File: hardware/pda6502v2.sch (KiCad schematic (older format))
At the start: 0 parts

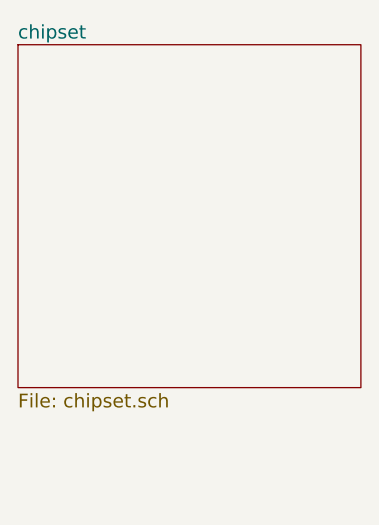
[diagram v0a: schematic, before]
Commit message: hardware: chipset hierarchical pins
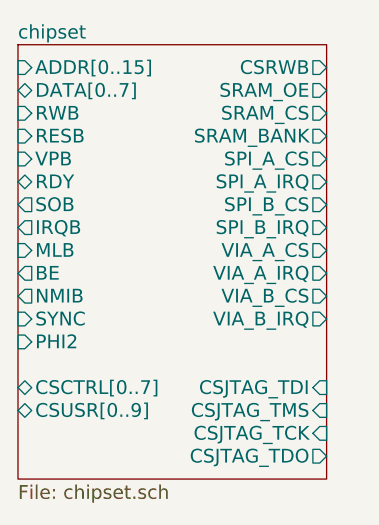
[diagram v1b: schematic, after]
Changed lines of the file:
@@
 $EndDescr
 $Sheet
-S 3400 2200 1500 1500
+S 3400 2200 1350 1900
 U 58EB910B
 F0 "chipset" 60
 F1 "chipset.sch" 60
+F2 "ADDR[0..15]" I L 3400 2300 60
+F3 "CSCTRL[0..7]" B L 3400 3700 60
+F4 "CSUSR[0..9]" B L 3400 3800 60
+F5 "RESB" I L 3400 2600 60
+F6 "VPB" I L 3400 2700 60
+F7 "RDY" B L 3400 2800 60
+F8 "SOB" O L 3400 2900 60
+F9 "IRQB" O L 3400 3000 60
+F10 "MLB" I L 3400 3100 60
+F11 "BE" O L 3400 3200 60
+F12 "NMIB" O L 3400 3300 60
+F13 "SYNC" I L 3400 3400 60
+F14 "RWB" I L 3400 2500 60
+F15 "PHI2" I L 3400 3500 60
+F16 "CSRWB" O R 4750 2300 60
+F17 "SRAM_OE" O R 4750 2400 60
+F18 "SRAM_CS" O R 4750 2500 60
+F19 "SRAM_BANK" O R 4750 2600 60
+F20 "SPI_A_CS" O R 4750 2700 60
+F21 "SPI_A_IRQ" O R 4750 2800 60
+F22 "SPI_B_CS" O R 4750 2900 60
+F23 "SPI_B_IRQ" O R 4750 3000 60
+F24 "VIA_A_CS" O R 4750 3100 60
+F25 "VIA_A_IRQ" O R 4750 3200 60
+F26 "VIA_B_CS" O R 4750 3300 60
+F27 "VIA_B_IRQ" O R 4750 3400 60
+F28 "CSJTAG_TDI" I R 4750 3700 60
+F29 "CSJTAG_TMS" I R 4750 3800 60
+F30 "CSJTAG_TCK" I R 4750 3900 60
+F31 "CSJTAG_TDO" O R 4750 4000 60
+F32 "DATA[0..7]" B L 3400 2400 60
 $EndSheet
 $EndSCHEMATC

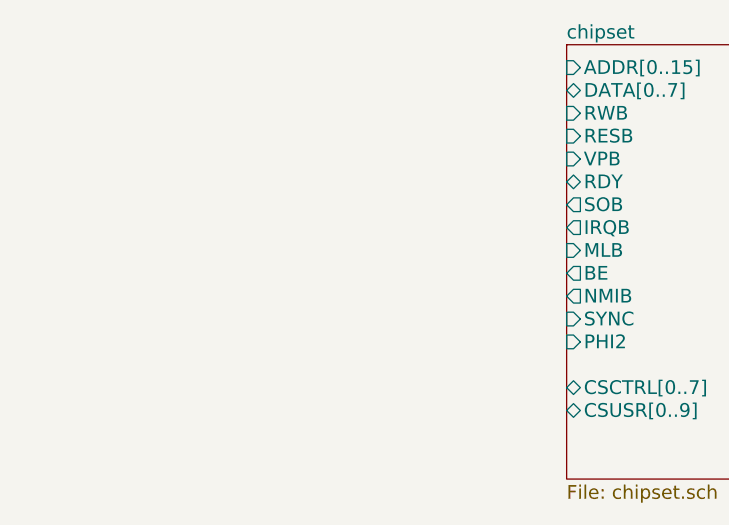
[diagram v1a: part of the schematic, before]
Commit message: hardware: CPU sub-schematic.
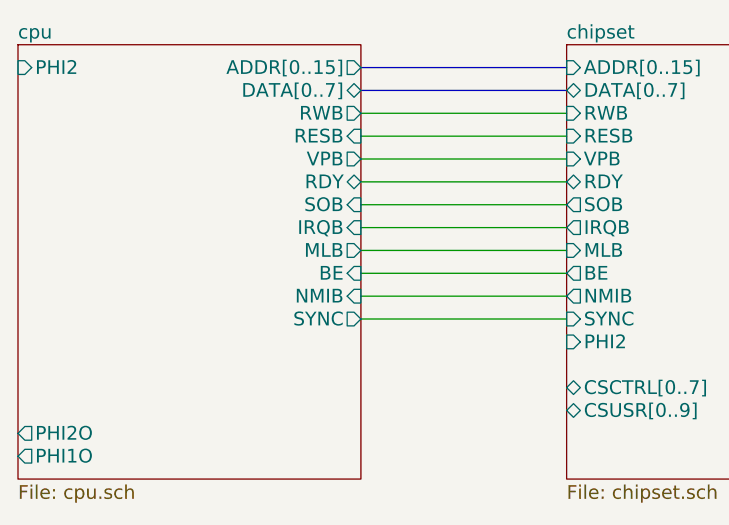
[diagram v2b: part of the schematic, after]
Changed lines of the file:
@@
 $Descr A4 11693 8268
 encoding utf-8
-Sheet 1 2
+Sheet 1 3
 Title ""
 Date ""
@@
 F32 "DATA[0..7]" B L 3400 2400 60
 $EndSheet
+$Sheet
+S 1000 2200 1500 1900
+U 58ED7217
+F0 "cpu" 60
+F1 "cpu.sch" 60
+F2 "ADDR[0..15]" O R 2500 2300 60
+F3 "DATA[0..7]" B R 2500 2400 60
+F4 "VPB" O R 2500 2700 60
+F5 "RDY" B R 2500 2800 60
+F6 "PHI1O" O L 1000 4000 60
+F7 "IRQB" I R 2500 3000 60
+F8 "MLB" O R 2500 3100 60
+F9 "NMIB" I R 2500 3300 60
+F10 "SYNC" O R 2500 3400 60
+F11 "RESB" I R 2500 2600 60
+F12 "PHI2O" O L 1000 3900 60
+F13 "SOB" I R 2500 2900 60
+F14 "PHI2" I L 1000 2300 60
+F15 "BE" I R 2500 3200 60
+F16 "RWB" O R 2500 2500 60
+$EndSheet
+Wire Bus Line
+	2500 2300 3400 2300
+Wire Bus Line
+	2500 2400 3400 2400
+Wire Wire Line
+	2500 2500 3400 2500
+Wire Wire Line
+	2500 2600 3400 2600
+Wire Wire Line
+	2500 2700 3400 2700
+Wire Wire Line
+	2500 2800 3400 2800
+Wire Wire Line
+	2500 2900 3400 2900
+Wire Wire Line
+	2500 3000 3400 3000
+Wire Wire Line
+	2500 3100 3400 3100
+Wire Wire Line
+	2500 3200 3400 3200
+Wire Wire Line
+	2500 3300 3400 3300
+Wire Wire Line
+	2500 3400 3400 3400
 $EndSCHEMATC

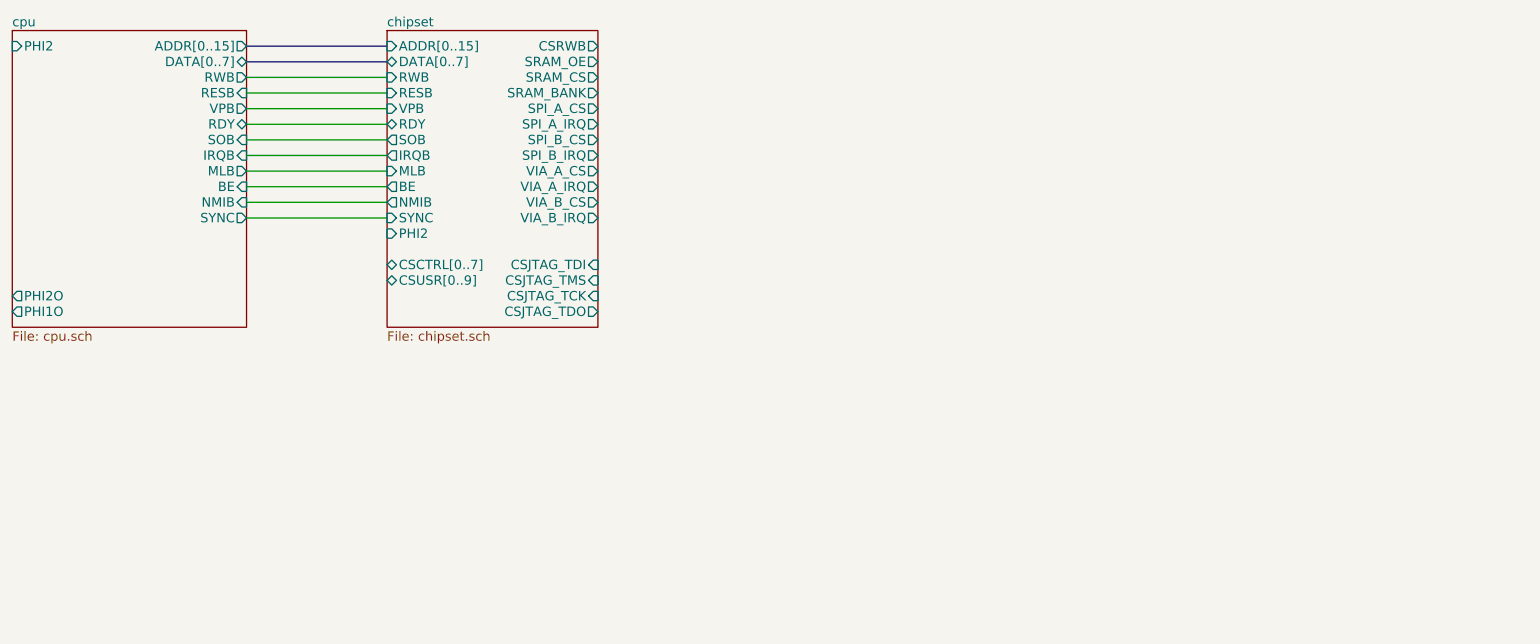
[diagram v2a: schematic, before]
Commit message: hardware: schematic for 2 x 6522 VIA/GPIO.
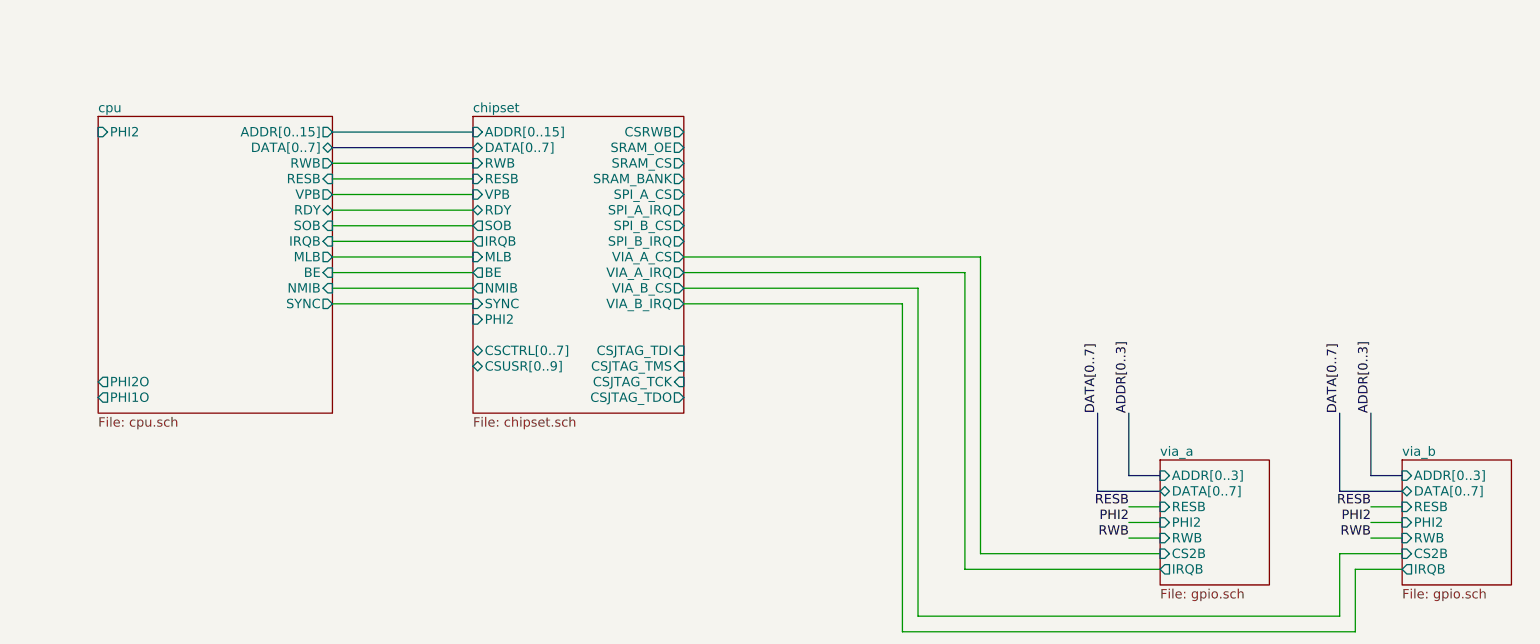
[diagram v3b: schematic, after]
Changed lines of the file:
@@
 $Descr A4 11693 8268
 encoding utf-8
-Sheet 1 3
+Sheet 1 5
 Title ""
 Date ""
@@
 $EndDescr
 $Sheet
-S 3400 2200 1350 1900
+S 3950 2750 1350 1900
 U 58EB910B
 F0 "chipset" 60
 F1 "chipset.sch" 60
-F2 "ADDR[0..15]" I L 3400 2300 60
-F3 "CSCTRL[0..7]" B L 3400 3700 60
-F4 "CSUSR[0..9]" B L 3400 3800 60
-F5 "RESB" I L 3400 2600 60
-F6 "VPB" I L 3400 2700 60
-F7 "RDY" B L 3400 2800 60
-F8 "SOB" O L 3400 2900 60
-F9 "IRQB" O L 3400 3000 60
-F10 "MLB" I L 3400 3100 60
-F11 "BE" O L 3400 3200 60
-F12 "NMIB" O L 3400 3300 60
-F13 "SYNC" I L 3400 3400 60
-F14 "RWB" I L 3400 2500 60
-F15 "PHI2" I L 3400 3500 60
-F16 "CSRWB" O R 4750 2300 60
-F17 "SRAM_OE" O R 4750 2400 60
-F18 "SRAM_CS" O R 4750 2500 60
-F19 "SRAM_BANK" O R 4750 2600 60
-F20 "SPI_A_CS" O R 4750 2700 60
-F21 "SPI_A_IRQ" O R 4750 2800 60
-F22 "SPI_B_CS" O R 4750 2900 60
-F23 "SPI_B_IRQ" O R 4750 3000 60
-F24 "VIA_A_CS" O R 4750 3100 60
-F25 "VIA_A_IRQ" O R 4750 3200 60
-F26 "VIA_B_CS" O R 4750 3300 60
-F27 "VIA_B_IRQ" O R 4750 3400 60
-F28 "CSJTAG_TDI" I R 4750 3700 60
-F29 "CSJTAG_TMS" I R 4750 3800 60
-F30 "CSJTAG_TCK" I R 4750 3900 60
-F31 "CSJTAG_TDO" O R 4750 4000 60
-F32 "DATA[0..7]" B L 3400 2400 60
-$EndSheet
-$Sheet
-S 1000 2200 1500 1900
+F2 "ADDR[0..15]" I L 3950 2850 60
+F3 "CSCTRL[0..7]" B L 3950 4250 60
+F4 "CSUSR[0..9]" B L 3950 4350 60
+F5 "RESB" I L 3950 3150 60
+F6 "VPB" I L 3950 3250 60
+F7 "RDY" B L 3950 3350 60
+F8 "SOB" O L 3950 3450 60
+F9 "IRQB" O L 3950 3550 60
+F10 "MLB" I L 3950 3650 60
+F11 "BE" O L 3950 3750 60
+F12 "NMIB" O L 3950 3850 60
+F13 "SYNC" I L 3950 3950 60
+F14 "RWB" I L 3950 3050 60
+F15 "PHI2" I L 3950 4050 60
+F16 "CSRWB" O R 5300 2850 60
+F17 "SRAM_OE" O R 5300 2950 60
+F18 "SRAM_CS" O R 5300 3050 60
+F19 "SRAM_BANK" O R 5300 3150 60
+F20 "SPI_A_CS" O R 5300 3250 60
+F21 "SPI_A_IRQ" O R 5300 3350 60
+F22 "SPI_B_CS" O R 5300 3450 60
+F23 "SPI_B_IRQ" O R 5300 3550 60
+F24 "VIA_A_CS" O R 5300 3650 60
+F25 "VIA_A_IRQ" O R 5300 3750 60
+F26 "VIA_B_CS" O R 5300 3850 60
+F27 "VIA_B_IRQ" O R 5300 3950 60
+F28 "CSJTAG_TDI" I R 5300 4250 60
+F29 "CSJTAG_TMS" I R 5300 4350 60
+F30 "CSJTAG_TCK" I R 5300 4450 60
+F31 "CSJTAG_TDO" O R 5300 4550 60
+F32 "DATA[0..7]" B L 3950 2950 60
+$EndSheet
+$Sheet
+S 1550 2750 1500 1900
 U 58ED7217
 F0 "cpu" 60
 F1 "cpu.sch" 60
-F2 "ADDR[0..15]" O R 2500 2300 60
-F3 "DATA[0..7]" B R 2500 2400 60
-F4 "VPB" O R 2500 2700 60
-F5 "RDY" B R 2500 2800 60
-F6 "PHI1O" O L 1000 4000 60
-F7 "IRQB" I R 2500 3000 60
-F8 "MLB" O R 2500 3100 60
-F9 "NMIB" I R 2500 3300 60
-F10 "SYNC" O R 2500 3400 60
-F11 "RESB" I R 2500 2600 60
-F12 "PHI2O" O L 1000 3900 60
-F13 "SOB" I R 2500 2900 60
-F14 "PHI2" I L 1000 2300 60
-F15 "BE" I R 2500 3200 60
-F16 "RWB" O R 2500 2500 60
-$EndSheet
-Wire Bus Line
-	2500 2300 3400 2300
-Wire Bus Line
-	2500 2400 3400 2400
-Wire Wire Line
-	2500 2500 3400 2500
-Wire Wire Line
-	2500 2600 3400 2600
-Wire Wire Line
-	2500 2700 3400 2700
-Wire Wire Line
-	2500 2800 3400 2800
-Wire Wire Line
-	2500 2900 3400 2900
-Wire Wire Line
-	2500 3000 3400 3000
-Wire Wire Line
-	2500 3100 3400 3100
-Wire Wire Line
-	2500 3200 3400 3200
-Wire Wire Line
-	2500 3300 3400 3300
-Wire Wire Line
-	2500 3400 3400 3400
+F2 "ADDR[0..15]" O R 3050 2850 60
+F3 "DATA[0..7]" B R 3050 2950 60
+F4 "VPB" O R 3050 3250 60
+F5 "RDY" B R 3050 3350 60
+F6 "PHI1O" O L 1550 4550 60
+F7 "IRQB" I R 3050 3550 60
+F8 "MLB" O R 3050 3650 60
+F9 "NMIB" I R 3050 3850 60
+F10 "SYNC" O R 3050 3950 60
+F11 "RESB" I R 3050 3150 60
+F12 "PHI2O" O L 1550 4450 60
+F13 "SOB" I R 3050 3450 60
+F14 "PHI2" I L 1550 2850 60
+F15 "BE" I R 3050 3750 60
+F16 "RWB" O R 3050 3050 60
+$EndSheet
+Wire Bus Line
+	3050 2850 3950 2850
+Wire Bus Line
+	3050 2950 3950 2950
+Wire Wire Line
+	3050 3050 3950 3050
+Wire Wire Line
+	3050 3150 3950 3150
+Wire Wire Line
+	3050 3250 3950 3250
+Wire Wire Line
+	3050 3350 3950 3350
+Wire Wire Line
+	3050 3450 3950 3450
+Wire Wire Line
+	3050 3550 3950 3550
+Wire Wire Line
+	3050 3650 3950 3650
+Wire Wire Line
+	3050 3750 3950 3750
+Wire Wire Line
+	3050 3850 3950 3850
+Wire Wire Line
+	3050 3950 3950 3950
+$Sheet
+S 9900 4950 700  800
+U 59012769
+F0 "via_b" 60
+F1 "gpio.sch" 60
+F2 "ADDR[0..3]" I L 9900 5050 60
+F3 "RESB" I L 9900 5250 60
+F4 "PHI2" I L 9900 5350 60
+F5 "RWB" I L 9900 5450 60
+F6 "CS2B" I L 9900 5550 60
+F7 "DATA[0..7]" B L 9900 5150 60
+F8 "IRQB" O L 9900 5650 60
+$EndSheet
+$Sheet
+S 8350 4950 700  800
+U 59009672
+F0 "via_a" 60
+F1 "gpio.sch" 60
+F2 "ADDR[0..3]" I L 8350 5050 60
+F3 "DATA[0..7]" B L 8350 5150 60
+F4 "RESB" I L 8350 5250 60
+F5 "PHI2" I L 8350 5350 60
+F6 "IRQB" O L 8350 5650 60
+F7 "RWB" I L 8350 5450 60
+F8 "CS2B" I L 8350 5550 60
+$EndSheet
+Wire Bus Line
+	8350 5050 8150 5050
+Wire Bus Line
+	8150 5050 8150 4650
+Wire Bus Line
+	8350 5150 7950 5150
+Wire Bus Line
+	7950 5150 7950 4650
+Wire Bus Line
+	9900 5050 9700 5050
+Wire Bus Line
+	9700 5050 9700 4650
+Wire Bus Line
+	9900 5150 9500 5150
+Wire Bus Line
+	9500 5150 9500 4650
+Wire Wire Line
+	8350 5250 8150 5250
+Text Label 8150 5250 2    60   ~ 0
+RESB
+Wire Wire Line
+	8350 5350 8150 5350
+Text Label 8150 5350 2    60   ~ 0
+PHI2
+Text Label 8150 5450 2    60   ~ 0
+RWB
+Wire Wire Line
+	8350 5450 8150 5450
+Wire Wire Line
+	9900 5250 9700 5250
+Wire Wire Line
+	9900 5350 9700 5350
+Wire Wire Line
+	9900 5450 9700 5450
+Text Label 9700 5250 2    60   ~ 0
+RESB
+Text Label 9700 5350 2    60   ~ 0
+PHI2
+Text Label 9700 5450 2    60   ~ 0
+RWB
+Text Label 7950 4650 1    60   ~ 0
+DATA[0..7]
+Text Label 8150 4650 1    60   ~ 0
+ADDR[0..3]
+Text Label 9500 4650 1    60   ~ 0
+DATA[0..7]
+Text Label 9700 4650 1    60   ~ 0
+ADDR[0..3]
+Wire Wire Line
+	5300 3650 7200 3650
+Wire Wire Line
+	7200 3650 7200 5550
+Wire Wire Line
+	7200 5550 8350 5550
+Wire Wire Line
+	5300 3750 7100 3750
+Wire Wire Line
+	7100 3750 7100 5650
+Wire Wire Line
+	7100 5650 8350 5650
+Wire Wire Line
+	5300 3850 6800 3850
+Wire Wire Line
+	6800 3850 6800 5950
+Wire Wire Line
+	6800 5950 9500 5950
+Wire Wire Line
+	9500 5950 9500 5550
+Wire Wire Line
+	9500 5550 9900 5550
+Wire Wire Line
+	5300 3950 6700 3950
+Wire Wire Line
+	6700 3950 6700 6050
+Wire Wire Line
+	6700 6050 9600 6050
+Wire Wire Line
+	9600 6050 9600 5650
+Wire Wire Line
+	9600 5650 9900 5650
 $EndSCHEMATC
